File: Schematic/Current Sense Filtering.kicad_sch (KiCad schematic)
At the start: 7 parts

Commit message: 1st Schematic Review
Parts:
- renumbered C16 to C19, C17 to C20, C18 to C21, R42 to R44, R43 to R45
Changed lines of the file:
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@@
 		(on_board yes)
 		(dnp no)
-		(property "Reference" "C18"
+		(property "Reference" "C21"
 			(at 160.02 94.234 90)
 			(effects
@@
 			(project "STAR"
 				(path "/fc8533bc-25dd-4c20-9b4c-ffebebd6739b/e8da5d81-614b-4fe5-84b3-4c351fab7114/ec6b8b52-e72f-4bdb-9407-1b78ccd1535b"
-					(reference "C18")
+					(reference "C21")
 					(unit 1)
 				)
@@
 		(on_board yes)
 		(dnp no)
-		(property "Reference" "R42"
+		(property "Reference" "R44"
 			(at 144.526 98.044 0)
 			(effects
@@
 			(project "STAR"
 				(path "/fc8533bc-25dd-4c20-9b4c-ffebebd6739b/e8da5d81-614b-4fe5-84b3-4c351fab7114/ec6b8b52-e72f-4bdb-9407-1b78ccd1535b"
-					(reference "R42")
+					(reference "R44")
 					(unit 1)
 				)
@@
 		(on_board yes)
 		(dnp no)
-		(property "Reference" "C17"
+		(property "Reference" "C20"
 			(at 147.32 94.234 90)
 			(effects
@@
 			(project "STAR"
 				(path "/fc8533bc-25dd-4c20-9b4c-ffebebd6739b/e8da5d81-614b-4fe5-84b3-4c351fab7114/ec6b8b52-e72f-4bdb-9407-1b78ccd1535b"
-					(reference "C17")
+					(reference "C20")
 					(unit 1)
 				)
@@
 		(on_board yes)
 		(dnp no)
-		(property "Reference" "#PWR015"
+		(property "Reference" "#PWR020"
 			(at 167.64 102.87 0)
 			(effects
@@
 			(project "STAR"
 				(path "/fc8533bc-25dd-4c20-9b4c-ffebebd6739b/e8da5d81-614b-4fe5-84b3-4c351fab7114/ec6b8b52-e72f-4bdb-9407-1b78ccd1535b"
-					(reference "#PWR015")
+					(reference "#PWR020")
 					(unit 1)
 				)
@@
 		(on_board yes)
 		(dnp no)
-		(property "Reference" "R43"
+		(property "Reference" "R45"
 			(at 157.226 98.044 0)
 			(effects
@@
 			(project "STAR"
 				(path "/fc8533bc-25dd-4c20-9b4c-ffebebd6739b/e8da5d81-614b-4fe5-84b3-4c351fab7114/ec6b8b52-e72f-4bdb-9407-1b78ccd1535b"
-					(reference "R43")
+					(reference "R45")
 					(unit 1)
 				)
@@
 		(on_board yes)
 		(dnp no)
-		(property "Reference" "C16"
+		(property "Reference" "C19"
 			(at 134.62 94.234 90)
 			(effects
@@
 			(project "STAR"
 				(path "/fc8533bc-25dd-4c20-9b4c-ffebebd6739b/e8da5d81-614b-4fe5-84b3-4c351fab7114/ec6b8b52-e72f-4bdb-9407-1b78ccd1535b"
-					(reference "C16")
+					(reference "C19")
 					(unit 1)
 				)
@@
 		(on_board yes)
 		(dnp no)
-		(property "Reference" "#PWR014"
+		(property "Reference" "#PWR019"
 			(at 129.54 102.87 0)
 			(effects
@@
 			(project "STAR"
 				(path "/fc8533bc-25dd-4c20-9b4c-ffebebd6739b/e8da5d81-614b-4fe5-84b3-4c351fab7114/ec6b8b52-e72f-4bdb-9407-1b78ccd1535b"
-					(reference "#PWR014")
+					(reference "#PWR019")
 					(unit 1)
 				)

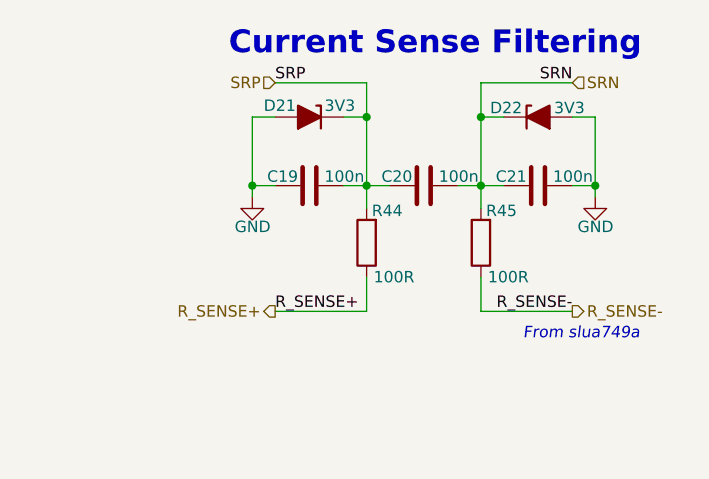
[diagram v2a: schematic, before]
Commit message: added so many test points
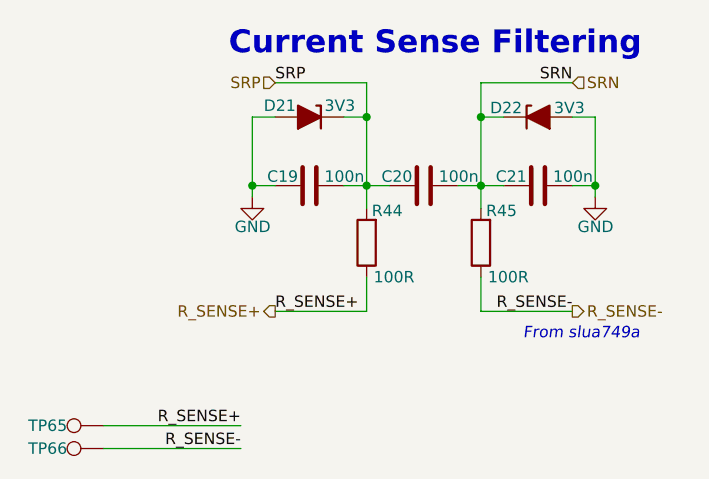
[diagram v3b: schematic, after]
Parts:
- added TP65, TP66: TestPoint, symbol Connector:TestPoint
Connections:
- net R_SENSE+: now also TP65.1
- net R_SENSE-: now also TP66.1
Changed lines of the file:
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@@
 	(wire
 		(pts
+			(xy 128.27 121.92) (xy 113.03 121.92)
+		)
+		(stroke
+			(width 0)
+			(type default)
+		)
+	)
+	(wire
+		(pts
 			(xy 142.24 105.41) (xy 142.24 109.22)
 		)
@@
 	(wire
 		(pts
+			(xy 128.27 124.46) (xy 113.03 124.46)
+		)
+		(stroke
+			(width 0)
+			(type default)
+		)
+	)
+	(wire
+		(pts
 			(xy 129.54 95.25) (xy 132.08 95.25)
 		)
@@
 	)
 	(label "R_SENSE-"
+		(at 128.27 124.46 180)
+		(effects
+			(font
+				(size 1.27 1.27)
+			)
+			(justify right bottom)
+		)
+	)
+	(label "R_SENSE-"
 		(at 165.1 109.22 180)
 		(effects
@@
 		)
 	)
+	(label "R_SENSE+"
+		(at 128.27 121.92 180)
+		(effects
+			(font
+				(size 1.27 1.27)
+			)
+			(justify right bottom)
+		)
+	)
 	(hierarchical_label "R_SENSE+"
 		(shape output)
@@
 	)
 	(symbol
+		(lib_id "Connector:TestPoint")
+		(at 113.03 121.92 90)
+		(unit 1)
+		(exclude_from_sim no)
+		(in_bom yes)
+		(on_board yes)
+		(dnp no)
+		(property "Reference" "TP65"
+			(at 108.966 121.92 90)
+			(effects
+				(font
+					(size 1.27 1.27)
+				)
+				(justify left)
+			)
+		)
+		(property "Value" "TestPoint"
+			(at 111.76 121.666 0)
+			(effects
+				(font
+					(size 1.27 1.27)
+				)
+				(justify left)
+				(hide yes)
+			)
+		)
+		(property "Footprint" ""
+			(at 113.03 116.84 0)
+			(effects
+				(font
+					(size 1.27 1.27)
+				)
+				(hide yes)
+			)
+		)
+		(property "Datasheet" "~"
+			(at 113.03 116.84 0)
+			(effects
+				(font
+					(size 1.27 1.27)
+				)
+				(hide yes)
+			)
+		)
+		(property "Description" "test point"
+			(at 113.03 121.92 0)
+			(effects
+				(font
+					(size 1.27 1.27)
+				)
+				(hide yes)
+			)
+		)
+		(pin "1"
+		)
+		(instances
+			(project "STAR"
+				(path "/fc8533bc-25dd-4c20-9b4c-ffebebd6739b/e8da5d81-614b-4fe5-84b3-4c351fab7114/ec6b8b52-e72f-4bdb-9407-1b78ccd1535b"
+					(reference "TP65")
+					(unit 1)
+				)
+			)
+		)
+	)
+	(symbol
 		(lib_id "power:GND")
 		(at 167.64 96.52 0)
@@
 		(on_board yes)
 		(dnp no)
-		(property "Reference" "#PWR020"
+		(property "Reference" "#PWR021"
 			(at 167.64 102.87 0)
 			(effects
@@
 			(project "STAR"
 				(path "/fc8533bc-25dd-4c20-9b4c-ffebebd6739b/e8da5d81-614b-4fe5-84b3-4c351fab7114/ec6b8b52-e72f-4bdb-9407-1b78ccd1535b"
-					(reference "#PWR020")
+					(reference "#PWR021")
 					(unit 1)
 				)
@@
 	)
 	(symbol
+		(lib_id "Connector:TestPoint")
+		(at 113.03 124.46 90)
+		(unit 1)
+		(exclude_from_sim no)
+		(in_bom yes)
+		(on_board yes)
+		(dnp no)
+		(property "Reference" "TP66"
+			(at 108.966 124.46 90)
+			(effects
+				(font
+					(size 1.27 1.27)
+				)
+				(justify left)
+			)
+		)
+		(property "Value" "TestPoint"
+			(at 111.76 124.206 0)
+			(effects
+				(font
+					(size 1.27 1.27)
+				)
+				(justify left)
+				(hide yes)
+			)
+		)
+		(property "Footprint" ""
+			(at 113.03 119.38 0)
+			(effects
+				(font
+					(size 1.27 1.27)
+				)
+				(hide yes)
+			)
+		)
+		(property "Datasheet" "~"
+			(at 113.03 119.38 0)
+			(effects
+				(font
+					(size 1.27 1.27)
+				)
+				(hide yes)
+			)
+		)
+		(property "Description" "test point"
+			(at 113.03 124.46 0)
+			(effects
+				(font
+					(size 1.27 1.27)
+				)
+				(hide yes)
+			)
+		)
+		(pin "1"
+		)
+		(instances
+			(project "STAR"
+				(path "/fc8533bc-25dd-4c20-9b4c-ffebebd6739b/e8da5d81-614b-4fe5-84b3-4c351fab7114/ec6b8b52-e72f-4bdb-9407-1b78ccd1535b"
+					(reference "TP66")
+					(unit 1)
+				)
+			)
+		)
+	)
+	(symbol
 		(lib_id "Device:C")
 		(at 135.89 95.25 90)
@@
 		(on_board yes)
 		(dnp no)
-		(property "Reference" "#PWR019"
+		(property "Reference" "#PWR020"
 			(at 129.54 102.87 0)
 			(effects
@@
 			(project "STAR"
 				(path "/fc8533bc-25dd-4c20-9b4c-ffebebd6739b/e8da5d81-614b-4fe5-84b3-4c351fab7114/ec6b8b52-e72f-4bdb-9407-1b78ccd1535b"
-					(reference "#PWR019")
+					(reference "#PWR020")
 					(unit 1)
 				)

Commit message: Added MCU
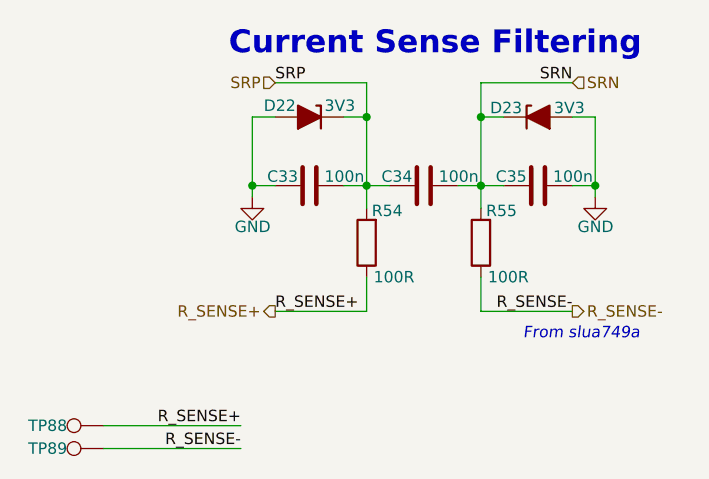
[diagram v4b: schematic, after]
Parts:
- renumbered C19 to C33, C20 to C34, C21 to C35, D21 to D22, D22 to D23, R44 to R54, R45 to R55, TP65 to TP88, TP66 to TP89
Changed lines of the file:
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@@
 		(on_board yes)
 		(dnp no)
-		(property "Reference" "C21"
+		(property "Reference" "C35"
 			(at 160.02 94.234 90)
 			(effects
@@
 			(project "STAR"
 				(path "/fc8533bc-25dd-4c20-9b4c-ffebebd6739b/e8da5d81-614b-4fe5-84b3-4c351fab7114/ec6b8b52-e72f-4bdb-9407-1b78ccd1535b"
-					(reference "C21")
+					(reference "C35")
 					(unit 1)
 				)
@@
 		(on_board yes)
 		(dnp no)
-		(property "Reference" "D21"
+		(property "Reference" "D22"
 			(at 134.366 86.36 0)
 			(effects
@@
 			(project "STAR"
 				(path "/fc8533bc-25dd-4c20-9b4c-ffebebd6739b/e8da5d81-614b-4fe5-84b3-4c351fab7114/ec6b8b52-e72f-4bdb-9407-1b78ccd1535b"
-					(reference "D21")
+					(reference "D22")
 					(unit 1)
 				)
@@
 		(on_board yes)
 		(dnp no)
-		(property "Reference" "R44"
+		(property "Reference" "R54"
 			(at 144.526 98.044 0)
 			(effects
@@
 			(project "STAR"
 				(path "/fc8533bc-25dd-4c20-9b4c-ffebebd6739b/e8da5d81-614b-4fe5-84b3-4c351fab7114/ec6b8b52-e72f-4bdb-9407-1b78ccd1535b"
-					(reference "R44")
+					(reference "R54")
 					(unit 1)
 				)
@@
 		(on_board yes)
 		(dnp no)
-		(property "Reference" "D22"
+		(property "Reference" "D23"
 			(at 155.956 86.614 0)
 			(effects
@@
 			(project "STAR"
 				(path "/fc8533bc-25dd-4c20-9b4c-ffebebd6739b/e8da5d81-614b-4fe5-84b3-4c351fab7114/ec6b8b52-e72f-4bdb-9407-1b78ccd1535b"
-					(reference "D22")
+					(reference "D23")
 					(unit 1)
 				)
@@
 		(on_board yes)
 		(dnp no)
-		(property "Reference" "C20"
+		(property "Reference" "C34"
 			(at 147.32 94.234 90)
 			(effects
@@
 			(project "STAR"
 				(path "/fc8533bc-25dd-4c20-9b4c-ffebebd6739b/e8da5d81-614b-4fe5-84b3-4c351fab7114/ec6b8b52-e72f-4bdb-9407-1b78ccd1535b"
-					(reference "C20")
+					(reference "C34")
 					(unit 1)
 				)
@@
 		(on_board yes)
 		(dnp no)
-		(property "Reference" "TP65"
+		(property "Reference" "TP88"
 			(at 108.966 121.92 90)
 			(effects
@@
 			(project "STAR"
 				(path "/fc8533bc-25dd-4c20-9b4c-ffebebd6739b/e8da5d81-614b-4fe5-84b3-4c351fab7114/ec6b8b52-e72f-4bdb-9407-1b78ccd1535b"
-					(reference "TP65")
+					(reference "TP88")
 					(unit 1)
 				)
@@
 		(on_board yes)
 		(dnp no)
-		(property "Reference" "#PWR021"
+		(property "Reference" "#PWR030"
 			(at 167.64 102.87 0)
 			(effects
@@
 			(project "STAR"
 				(path "/fc8533bc-25dd-4c20-9b4c-ffebebd6739b/e8da5d81-614b-4fe5-84b3-4c351fab7114/ec6b8b52-e72f-4bdb-9407-1b78ccd1535b"
-					(reference "#PWR021")
+					(reference "#PWR030")
 					(unit 1)
 				)
@@
 		(on_board yes)
 		(dnp no)
-		(property "Reference" "R45"
+		(property "Reference" "R55"
 			(at 157.226 98.044 0)
 			(effects
@@
 			(project "STAR"
 				(path "/fc8533bc-25dd-4c20-9b4c-ffebebd6739b/e8da5d81-614b-4fe5-84b3-4c351fab7114/ec6b8b52-e72f-4bdb-9407-1b78ccd1535b"
-					(reference "R45")
+					(reference "R55")
 					(unit 1)
 				)
@@
 		(on_board yes)
 		(dnp no)
-		(property "Reference" "TP66"
+		(property "Reference" "TP89"
 			(at 108.966 124.46 90)
 			(effects
@@
 			(project "STAR"
 				(path "/fc8533bc-25dd-4c20-9b4c-ffebebd6739b/e8da5d81-614b-4fe5-84b3-4c351fab7114/ec6b8b52-e72f-4bdb-9407-1b78ccd1535b"
-					(reference "TP66")
+					(reference "TP89")
 					(unit 1)
 				)
@@
 		(on_board yes)
 		(dnp no)
-		(property "Reference" "C19"
+		(property "Reference" "C33"
 			(at 134.62 94.234 90)
 			(effects
@@
 			(project "STAR"
 				(path "/fc8533bc-25dd-4c20-9b4c-ffebebd6739b/e8da5d81-614b-4fe5-84b3-4c351fab7114/ec6b8b52-e72f-4bdb-9407-1b78ccd1535b"
-					(reference "C19")
+					(reference "C33")
 					(unit 1)
 				)
@@
 		(on_board yes)
 		(dnp no)
-		(property "Reference" "#PWR020"
+		(property "Reference" "#PWR029"
 			(at 129.54 102.87 0)
 			(effects
@@
 			(project "STAR"
 				(path "/fc8533bc-25dd-4c20-9b4c-ffebebd6739b/e8da5d81-614b-4fe5-84b3-4c351fab7114/ec6b8b52-e72f-4bdb-9407-1b78ccd1535b"
-					(reference "#PWR020")
+					(reference "#PWR029")
 					(unit 1)
 				)

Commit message: Started to work on the BOM
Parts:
- removed D22, D23: 3V3, symbol Device:D_Zener_Filled
- C28: renamed from C33; footprint (none) -> Capacitor_SMD:C_1206_3216Metric_Pad1.33x1.80mm_HandSolder; Link (none) -> https://mou.sr/4n9ybmQ; Manufacturer Part Number (none) -> CL31B104KBCNNNC; Price per Unit (none) -> 0.11; Supplier (none) -> Mouser; Supplier Part Number (none) -> 187-CL31B104KBCNNNC
- C29: renamed from C34; footprint (none) -> Capacitor_SMD:C_1206_3216Metric_Pad1.33x1.80mm_HandSolder; Link (none) -> https://mou.sr/4n9ybmQ; Manufacturer Part Number (none) -> CL31B104KBCNNNC; Price per Unit (none) -> 0.11; Supplier (none) -> Mouser; Supplier Part Number (none) -> 187-CL31B104KBCNNNC
- C30: renamed from C35; footprint (none) -> Capacitor_SMD:C_1206_3216Metric_Pad1.33x1.80mm_HandSolder; Link (none) -> https://mou.sr/4n9ybmQ; Manufacturer Part Number (none) -> CL31B104KBCNNNC; Price per Unit (none) -> 0.11; Supplier (none) -> Mouser; Supplier Part Number (none) -> 187-CL31B104KBCNNNC
- renumbered R54 to R50, R55 to R51, TP88 to TP65, TP89 to TP66

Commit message: Massive pivit, simplification
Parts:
- renumbered C28 to C21, C29 to C22, C30 to C23, TP65 to TP58, TP66 to TP59
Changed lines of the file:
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@@
 		(on_board yes)
 		(dnp no)
-		(property "Reference" "C30"
+		(property "Reference" "C23"
 			(at 160.02 94.234 90)
 			(effects
@@
 		)
 		(property "Sim.Pins" ""
+			(at 161.29 95.25 90)
+			(effects
+				(font
+					(size 1.27 1.27)
+				)
+				(hide yes)
+			)
+		)
+		(property "SNAPEDA_PACKAGE_ID" ""
 			(at 161.29 95.25 90)
 			(effects
@@
 			(project "STAR"
 				(path "/fc8533bc-25dd-4c20-9b4c-ffebebd6739b/e8da5d81-614b-4fe5-84b3-4c351fab7114/ec6b8b52-e72f-4bdb-9407-1b78ccd1535b"
-					(reference "C30")
+					(reference "C23")
 					(unit 1)
 				)
@@
 			)
 		)
+		(property "SNAPEDA_PACKAGE_ID" ""
+			(at 142.24 101.6 0)
+			(effects
+				(font
+					(size 1.27 1.27)
+				)
+				(hide yes)
+			)
+		)
 		(pin "1"
 		)
@@
 		(on_board yes)
 		(dnp no)
-		(property "Reference" "C29"
+		(property "Reference" "C22"
 			(at 147.32 94.234 90)
 			(effects
@@
 		)
 		(property "Sim.Pins" ""
+			(at 148.59 95.25 90)
+			(effects
+				(font
+					(size 1.27 1.27)
+				)
+				(hide yes)
+			)
+		)
+		(property "SNAPEDA_PACKAGE_ID" ""
 			(at 148.59 95.25 90)
 			(effects
@@
 			(project "STAR"
 				(path "/fc8533bc-25dd-4c20-9b4c-ffebebd6739b/e8da5d81-614b-4fe5-84b3-4c351fab7114/ec6b8b52-e72f-4bdb-9407-1b78ccd1535b"
-					(reference "C29")
+					(reference "C22")
 					(unit 1)
 				)
@@
 		(on_board yes)
 		(dnp no)
-		(property "Reference" "TP65"
+		(property "Reference" "TP58"
 			(at 108.966 121.92 90)
 			(effects
@@
 		)
 		(property "Sim.Pins" ""
+			(at 113.03 121.92 90)
+			(effects
+				(font
+					(size 1.27 1.27)
+				)
+				(hide yes)
+			)
+		)
+		(property "SNAPEDA_PACKAGE_ID" ""
 			(at 113.03 121.92 90)
 			(effects
@@
 			(project "STAR"
 				(path "/fc8533bc-25dd-4c20-9b4c-ffebebd6739b/e8da5d81-614b-4fe5-84b3-4c351fab7114/ec6b8b52-e72f-4bdb-9407-1b78ccd1535b"
-					(reference "TP65")
+					(reference "TP58")
 					(unit 1)
 				)
@@
 		(on_board yes)
 		(dnp no)
-		(property "Reference" "#PWR025"
+		(property "Reference" "#PWR014"
 			(at 167.64 102.87 0)
 			(effects
@@
 			(project "STAR"
 				(path "/fc8533bc-25dd-4c20-9b4c-ffebebd6739b/e8da5d81-614b-4fe5-84b3-4c351fab7114/ec6b8b52-e72f-4bdb-9407-1b78ccd1535b"
-					(reference "#PWR025")
+					(reference "#PWR014")
 					(unit 1)
 				)
@@
 			)
 		)
+		(property "SNAPEDA_PACKAGE_ID" ""
+			(at 154.94 101.6 0)
+			(effects
+				(font
+					(size 1.27 1.27)
+				)
+				(hide yes)
+			)
+		)
 		(pin "1"
 		)
@@
 		(on_board yes)
 		(dnp no)
-		(property "Reference" "TP66"
+		(property "Reference" "TP59"
 			(at 108.966 124.46 90)
 			(effects
@@
 		)
 		(property "Sim.Pins" ""
+			(at 113.03 124.46 90)
+			(effects
+				(font
+					(size 1.27 1.27)
+				)
+				(hide yes)
+			)
+		)
+		(property "SNAPEDA_PACKAGE_ID" ""
 			(at 113.03 124.46 90)
 			(effects
@@
 			(project "STAR"
 				(path "/fc8533bc-25dd-4c20-9b4c-ffebebd6739b/e8da5d81-614b-4fe5-84b3-4c351fab7114/ec6b8b52-e72f-4bdb-9407-1b78ccd1535b"
-					(reference "TP66")
+					(reference "TP59")
 					(unit 1)
 				)
@@
 		(on_board yes)
 		(dnp no)
-		(property "Reference" "C28"
+		(property "Reference" "C21"
 			(at 134.62 94.234 90)
 			(effects
@@
 		)
 		(property "Sim.Pins" ""
+			(at 135.89 95.25 90)
+			(effects
+				(font
+					(size 1.27 1.27)
+				)
+				(hide yes)
+			)
+		)
+		(property "SNAPEDA_PACKAGE_ID" ""
 			(at 135.89 95.25 90)
 			(effects
@@
 			(project "STAR"
 				(path "/fc8533bc-25dd-4c20-9b4c-ffebebd6739b/e8da5d81-614b-4fe5-84b3-4c351fab7114/ec6b8b52-e72f-4bdb-9407-1b78ccd1535b"
-					(reference "C28")
+					(reference "C21")
 					(unit 1)
 				)
@@
 		(on_board yes)
 		(dnp no)
-		(property "Reference" "#PWR024"
+		(property "Reference" "#PWR013"
 			(at 129.54 102.87 0)
 			(effects
@@
 			(project "STAR"
 				(path "/fc8533bc-25dd-4c20-9b4c-ffebebd6739b/e8da5d81-614b-4fe5-84b3-4c351fab7114/ec6b8b52-e72f-4bdb-9407-1b78ccd1535b"
-					(reference "#PWR024")
+					(reference "#PWR013")
 					(unit 1)
 				)
